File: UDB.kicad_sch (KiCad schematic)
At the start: 14 parts, among them J1 TYPE-C-31-M12_13, J2 SM04B-SRSS-TB(LF)(SN), U1 TPD4E05U06DQAR

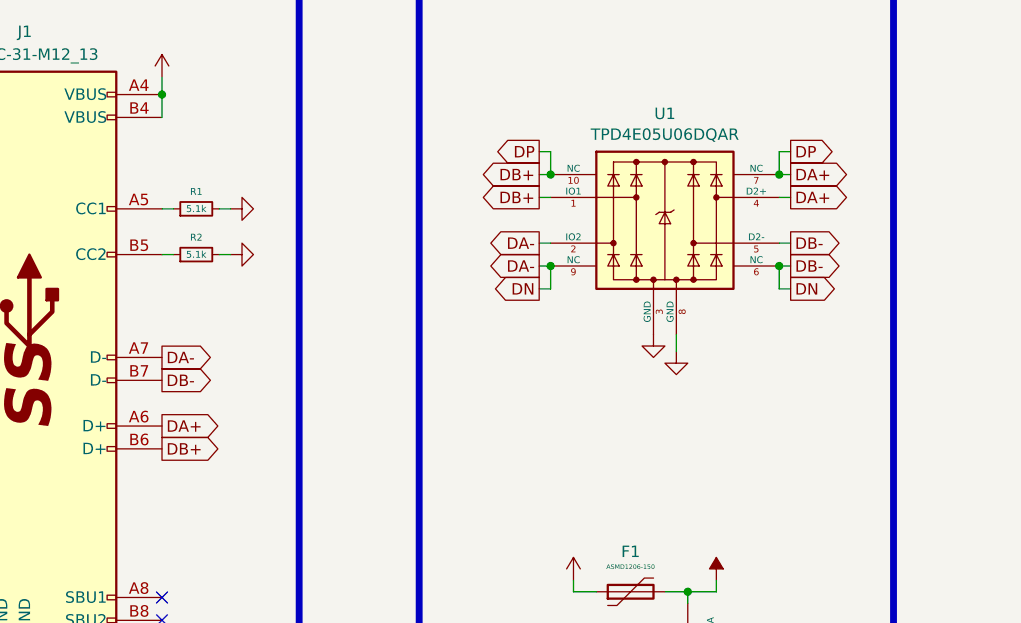
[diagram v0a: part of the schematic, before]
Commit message: Skew phase adjustment for outer USB diff pair
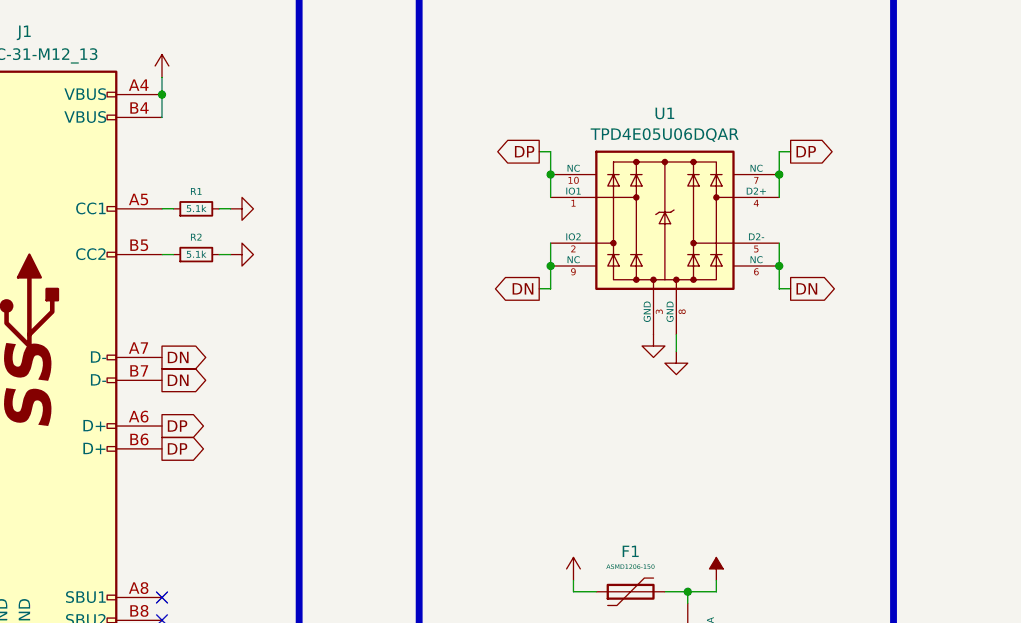
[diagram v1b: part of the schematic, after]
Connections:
- net DA+ renamed DP
- net DA- renamed DN
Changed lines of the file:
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@@
     (company "Designed by the keyboard community")
   )
+  (junction (at 98.425 38.735) (diameter 0) (color 0 0 0 0)
+  )
   (junction (at 98.425 48.895) (diameter 0) (color 0 0 0 0)
   )
+  (junction (at 55.245 29.845) (diameter 0) (color 0 0 0 0)
+  )
+  (junction (at 113.665 85.09) (diameter 0) (color 0 0 0 0)
+  )
   (junction (at 123.825 38.735) (diameter 0) (color 0 0 0 0)
   )
-  (junction (at 98.425 38.735) (diameter 0) (color 0 0 0 0)
-  )
   (junction (at 123.825 48.895) (diameter 0) (color 0 0 0 0)
-  )
-  (junction (at 55.245 29.845) (diameter 0) (color 0 0 0 0)
-  )
-  (junction (at 113.665 85.09) (diameter 0) (color 0 0 0 0)
   )
   (no_connect (at 55.245 85.725))
@@
     (stroke (width 0) (type default) (color 0 0 0 0))
   )
+  (wire (pts (xy 98.425 38.735) (xy 98.425 41.275))
+    (stroke (width 0) (type default) (color 0 0 0 0))
+  )
   (wire (pts (xy 111.125 85.09) (xy 113.665 85.09))
     (stroke (width 0) (type default) (color 0 0 0 0))
   )
-  (wire (pts (xy 123.825 38.735) (xy 125.095 38.735))
+  (wire (pts (xy 123.825 38.735) (xy 123.825 41.275))
     (stroke (width 0) (type default) (color 0 0 0 0))
   )
@@
     (stroke (width 0) (type default) (color 0 0 0 0))
   )
-  (wire (pts (xy 123.825 48.895) (xy 125.095 48.895))
-    (stroke (width 0) (type default) (color 0 0 0 0))
-  )
   (wire (pts (xy 113.665 93.98) (xy 113.665 95.885))
     (stroke (width 0) (type default) (color 0 0 0 0))
@@
     (stroke (width 0) (type default) (color 0 0 0 0))
   )
-  (wire (pts (xy 97.155 38.735) (xy 98.425 38.735))
+  (wire (pts (xy 123.825 46.355) (xy 123.825 48.895))
     (stroke (width 0) (type default) (color 0 0 0 0))
   )
@@
     (stroke (width 0) (type default) (color 0 0 0 0))
   )
-  (wire (pts (xy 97.155 46.355) (xy 98.425 46.355))
-    (stroke (width 0) (type default) (color 0 0 0 0))
-  )
   (wire (pts (xy 55.245 29.845) (xy 55.245 32.385))
     (stroke (width 0) (type default) (color 0 0 0 0))
@@
     (stroke (width 0.762) (type default) (color 0 0 0 0))
   )
-  (wire (pts (xy 123.825 46.355) (xy 125.095 46.355))
-    (stroke (width 0) (type default) (color 0 0 0 0))
-  )
   (wire (pts (xy 55.245 27.94) (xy 55.245 29.845))
     (stroke (width 0) (type default) (color 0 0 0 0))
@@
     (stroke (width 0.762) (type default) (color 0 0 0 0))
   )
-  (wire (pts (xy 123.825 41.275) (xy 125.095 41.275))
-    (stroke (width 0) (type default) (color 0 0 0 0))
-  )
   (wire (pts (xy 98.425 51.435) (xy 98.425 48.895))
     (stroke (width 0) (type default) (color 0 0 0 0))
   )
-  (wire (pts (xy 97.155 41.275) (xy 98.425 41.275))
+  (wire (pts (xy 98.425 46.355) (xy 98.425 48.895))
     (stroke (width 0) (type default) (color 0 0 0 0))
   )
@@
     (stroke (width 0.762) (type default) (color 0 0 0 0))
   )
-  (wire (pts (xy 97.155 48.895) (xy 98.425 48.895))
-    (stroke (width 0) (type default) (color 0 0 0 0))
-  )
   (wire (pts (xy 113.665 85.09) (xy 113.665 86.36))
     (stroke (width 0) (type default) (color 0 0 0 0))
@@
     (effects (font (size 5.08 5.08) (thickness 1.016) bold) (justify right bottom))
   )
-  (global_label "DB-" (shape output) (at 125.095 48.895 0) (fields_autoplaced)
+  (global_label "DN" (shape output) (at 55.245 59.055 0) (fields_autoplaced)
+    (effects (font (size 1.27 1.27)) (justify left))
+    (property "Intersheet References" "${INTERSHEET_REFS}" (id 0) (at 152.4 110.49 0)
+      (effects (font (size 1.27 1.27)) hide)
+    )
+  )
+  (global_label "DN" (shape output) (at 55.245 61.595 0) (fields_autoplaced)
+    (effects (font (size 1.27 1.27)) (justify left))
+    (property "Intersheet References" "${INTERSHEET_REFS}" (id 0) (at 152.4 113.03 0)
+      (effects (font (size 1.27 1.27)) hide)
+    )
+  )
+  (global_label "DN" (shape output) (at 125.095 51.435 0) (fields_autoplaced)
     (effects (font (size 1.27 1.27)) (justify left))
     (property "Intersheet References" "${INTERSHEET_REFS}" (id 0) (at 0 0 0)
@@
     )
   )
-  (global_label "DB-" (shape output) (at 55.245 61.595 0) (fields_autoplaced)
-    (effects (font (size 1.27 1.27)) (justify left))
-    (property "Intersheet References" "${INTERSHEET_REFS}" (id 0) (at 0 0 0)
-      (effects (font (size 1.27 1.27)) hide)
-    )
-  )
-  (global_label "DA-" (shape output) (at 97.155 48.895 180) (fields_autoplaced)
-    (effects (font (size 1.27 1.27)) (justify right))
-    (property "Intersheet References" "${INTERSHEET_REFS}" (id 0) (at 0 0 0)
-      (effects (font (size 1.27 1.27)) hide)
-    )
-  )
-  (global_label "DA+" (shape output) (at 125.095 38.735 0) (fields_autoplaced)
-    (effects (font (size 1.27 1.27)) (justify left))
-    (property "Intersheet References" "${INTERSHEET_REFS}" (id 0) (at 0 0 0)
-      (effects (font (size 1.27 1.27)) hide)
-    )
-  )
-  (global_label "DB-" (shape output) (at 125.095 46.355 0) (fields_autoplaced)
-    (effects (font (size 1.27 1.27)) (justify left))
-    (property "Intersheet References" "${INTERSHEET_REFS}" (id 0) (at 0 0 0)
-      (effects (font (size 1.27 1.27)) hide)
-    )
-  )
-  (global_label "DN" (shape output) (at 125.095 51.435 0) (fields_autoplaced)
-    (effects (font (size 1.27 1.27)) (justify left))
-    (property "Intersheet References" "${INTERSHEET_REFS}" (id 0) (at 0 0 0)
-      (effects (font (size 1.27 1.27)) hide)
-    )
-  )
-  (global_label "DA+" (shape output) (at 55.245 66.675 0) (fields_autoplaced)
-    (effects (font (size 1.27 1.27)) (justify left))
-    (property "Intersheet References" "${INTERSHEET_REFS}" (id 0) (at 0 0 0)
-      (effects (font (size 1.27 1.27)) hide)
-    )
-  )
-  (global_label "DA+" (shape output) (at 125.095 41.275 0) (fields_autoplaced)
-    (effects (font (size 1.27 1.27)) (justify left))
-    (property "Intersheet References" "${INTERSHEET_REFS}" (id 0) (at 0 0 0)
-      (effects (font (size 1.27 1.27)) hide)
-    )
-  )
-  (global_label "DB+" (shape output) (at 97.155 38.735 180) (fields_autoplaced)
-    (effects (font (size 1.27 1.27)) (justify right))
-    (property "Intersheet References" "${INTERSHEET_REFS}" (id 0) (at 0 0 0)
-      (effects (font (size 1.27 1.27)) hide)
-    )
-  )
-  (global_label "DA-" (shape output) (at 97.155 46.355 180) (fields_autoplaced)
-    (effects (font (size 1.27 1.27)) (justify right))
-    (property "Intersheet References" "${INTERSHEET_REFS}" (id 0) (at 0 0 0)
+  (global_label "DP" (shape output) (at 55.245 69.215 0) (fields_autoplaced)
+    (effects (font (size 1.27 1.27)) (justify left))
+    (property "Intersheet References" "${INTERSHEET_REFS}" (id 0) (at 152.4 105.41 0)
       (effects (font (size 1.27 1.27)) hide)
     )
@@
     )
   )
-  (global_label "DA-" (shape output) (at 55.245 59.055 0) (fields_autoplaced)
-    (effects (font (size 1.27 1.27)) (justify left))
-    (property "Intersheet References" "${INTERSHEET_REFS}" (id 0) (at 0 0 0)
-      (effects (font (size 1.27 1.27)) hide)
-    )
-  )
-  (global_label "DB+" (shape output) (at 55.245 69.215 0) (fields_autoplaced)
-    (effects (font (size 1.27 1.27)) (justify left))
-    (property "Intersheet References" "${INTERSHEET_REFS}" (id 0) (at 0 0 0)
+  (global_label "DP" (shape output) (at 55.245 66.675 0) (fields_autoplaced)
+    (effects (font (size 1.27 1.27)) (justify left))
+    (property "Intersheet References" "${INTERSHEET_REFS}" (id 0) (at 152.4 102.87 0)
       (effects (font (size 1.27 1.27)) hide)
     )
@@
     (effects (font (size 1.27 1.27)) (justify right))
     (property "Intersheet References" "${INTERSHEET_REFS}" (id 0) (at 0 0 0)
-      (effects (font (size 1.27 1.27)) hide)
-    )
-  )
-  (global_label "DB+" (shape output) (at 97.155 41.275 180) (fields_autoplaced)
-    (effects (font (size 1.27 1.27)) (justify right))
-    (property "Intersheet References" "${INTERSHEET_REFS}" (id 0) (at 0 0 0)

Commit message: Edit component metadata, final checks, release
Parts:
- J1: LCSC Part No C165948 -> (none); LCSC Part Number (none) -> C165948; Manufacturer Part No TYPE-C-31-M-12 -> (none); Manufacturer Part Number (none) -> TYPE-C-31-M-12
- J2: value SM04B-SRSS-TB(LF)(SN) -> X1224WRS-04-LPV01; LCSC Part No C160404 -> (none); LCSC Part Number (none) -> C528030; Manufacturer JST Sales America -> XKB Connectivity; Manufacturer Part No SM04B-SRSS-TB(LF)(SN) -> (none); Manufacturer Part Number (none) -> X1224WRS-04-LPV01
- L1: LCSC Part No C33600 -> (none); LCSC Part Number (none) -> C33600; Manufacturer Part No MLB3216-600P4A(f) -> (none); Manufacturer Part Number (none) -> MLB3216-600P4A(f)
- R1: LCSC Part Number (none) -> C25905; Manufacturer (none) -> Uniroyal; Manufacturer Part Number (none) -> 0402WGF5101TCE
- U1: LCSC Part No C138714 -> (none); LCSC Part Number (none) -> C138714; Manufacturer Part No TPD4E05U06DQAR -> (none); Manufacturer Part Number (none) -> TPD4E05U06DQAR
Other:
- company: Designed by the keyboard community -> Designed by the UDB team

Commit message: Swap footprint
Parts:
- J2: footprint acheron_Connectors:MOLEX_781710004_MountingReliefs -> locallib:PicoEZMate-Reinforced-Alt
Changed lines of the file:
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@@
       (effects (font (size 1.27 1.27)) (justify left))
     )
-    (property "Footprint" "acheron_Connectors:MOLEX_781710004_MountingReliefs" (id 2) (at 241.3 77.47 0)
+    (property "Footprint" "locallib:PicoEZMate-Reinforced-Alt" (id 2) (at 241.3 77.47 0)
       (effects (font (size 1.27 1.27)) hide)
     )
@@
     )
     (path "/00000000-0000-0000-0000-00005c91afcb"
-      (reference "J2") (unit 1) (value "X1224WRS-04-LPV01") (footprint "acheron_Connectors:MOLEX_781710004_MountingReliefs")
+      (reference "J2") (unit 1) (value "X1224WRS-04-LPV01") (footprint "locallib:PicoEZMate-Reinforced-Alt")
     )
     (path "/00000000-0000-0000-0000-00005e78ff8f"

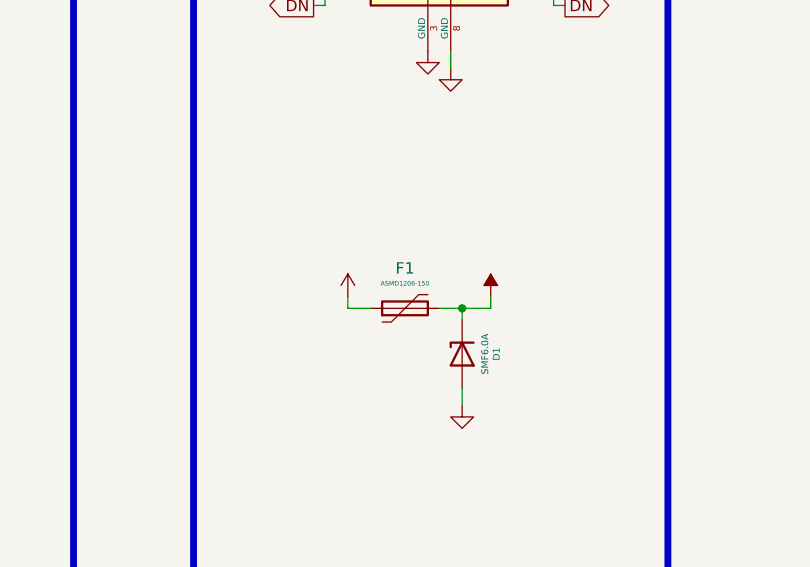
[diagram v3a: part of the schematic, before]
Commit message: fix BOM file and use correct manufacturer part num for fuse
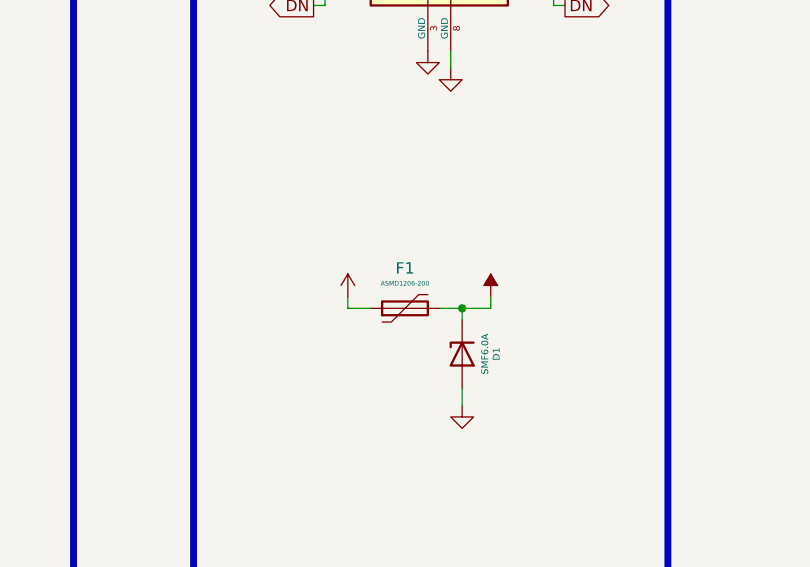
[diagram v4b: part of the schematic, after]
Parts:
- F1: value ASMD1206-150 -> ASMD1206-200; Manufacturer Part Number ASMD1206-150 -> ASMD1206-200
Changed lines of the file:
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@@
     (in_bom yes) (on_board yes)
     (property "Reference" "F1" (id 0) (at 107.315 80.645 90))
-    (property "Value" "ASMD1206-150" (id 1) (at 107.315 82.3214 90)
+    (property "Value" "ASMD1206-200" (id 1) (at 107.315 82.3214 90)
       (effects (font (size 0.508 0.508)))
     )
@@
       (effects (font (size 1.27 1.27)) hide)
     )
-    (property "Manufacturer Part Number" "ASMD1206-150" (id 5) (at 107.315 85.09 90)
+    (property "Manufacturer Part Number" "ASMD1206-200" (id 5) (at 107.315 85.09 90)
       (effects (font (size 1.27 1.27)) hide)
     )
@@
     )
     (path "/00000000-0000-0000-0000-00005e78a38e"
-      (reference "F1") (unit 1) (value "ASMD1206-150") (footprint "Fuse:Fuse_1206_3216Metric")
+      (reference "F1") (unit 1) (value "ASMD1206-200") (footprint "Fuse:Fuse_1206_3216Metric")
     )
     (path "/00000000-0000-0000-0000-00005e790861"
